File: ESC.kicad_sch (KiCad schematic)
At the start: 2 parts, among them U5 STM32G071GBUxN

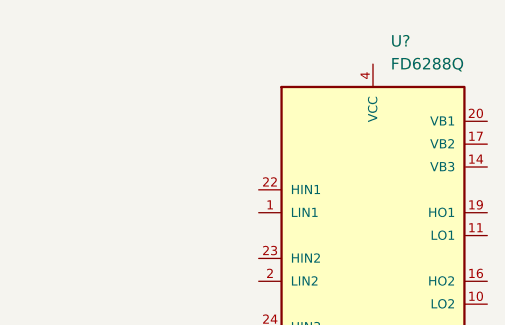
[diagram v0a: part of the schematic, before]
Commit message: Receiver design
Updated the receiver design for the SX1280.
Added an ignore for lock files.
Minor schematic updates.
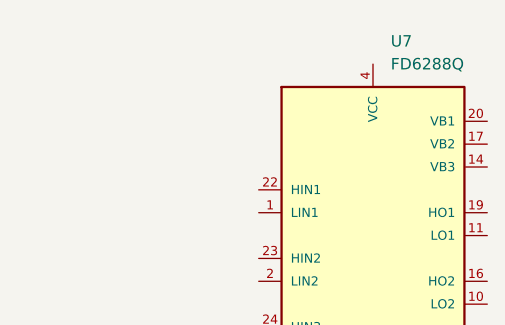
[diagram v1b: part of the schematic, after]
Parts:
- U5: footprint Package_DFN_QFN:QFN-28_4x4mm_P0.5mm -> Custom_Parts:QFN-28_4x4mm_P0.5mm
- gave numbers to parts that had none: 1
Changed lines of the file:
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@@
 		(dnp no)
 		(fields_autoplaced yes)
-		(property "Reference" "U?"
+		(property "Reference" "U7"
 			(at 123.8886 34.29 0)
 			(effects
@@
 			(project "ThunderHorse"
 				(path "/ac187c6c-fa53-41cc-bce1-6f39a42a92e8/807a5f6f-4255-4cf0-8d90-acd62bb18590"
-					(reference "U?")
+					(reference "U7")
 					(unit 1)
 				)
@@
 			)
 		)
-		(property "Footprint" "Package_DFN_QFN:QFN-28_4x4mm_P0.5mm"
+		(property "Footprint" "Custom_Parts:QFN-28_4x4mm_P0.5mm"
 			(at 44.45 86.36 0)
 			(effects

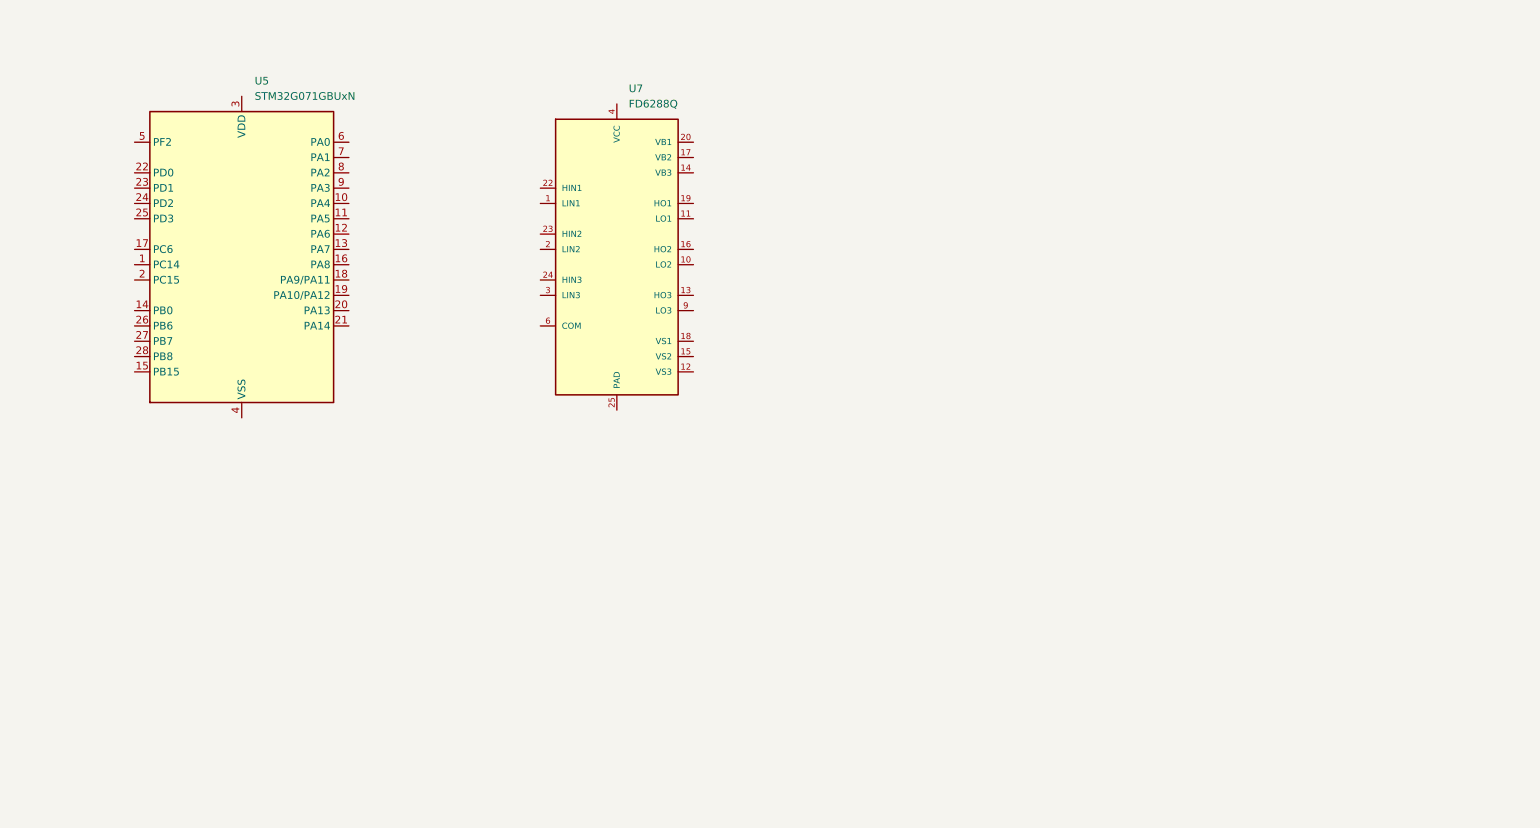
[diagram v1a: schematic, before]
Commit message: ESC design
Updated the ESC schematic.
Replaces the INA 226 with INA230.
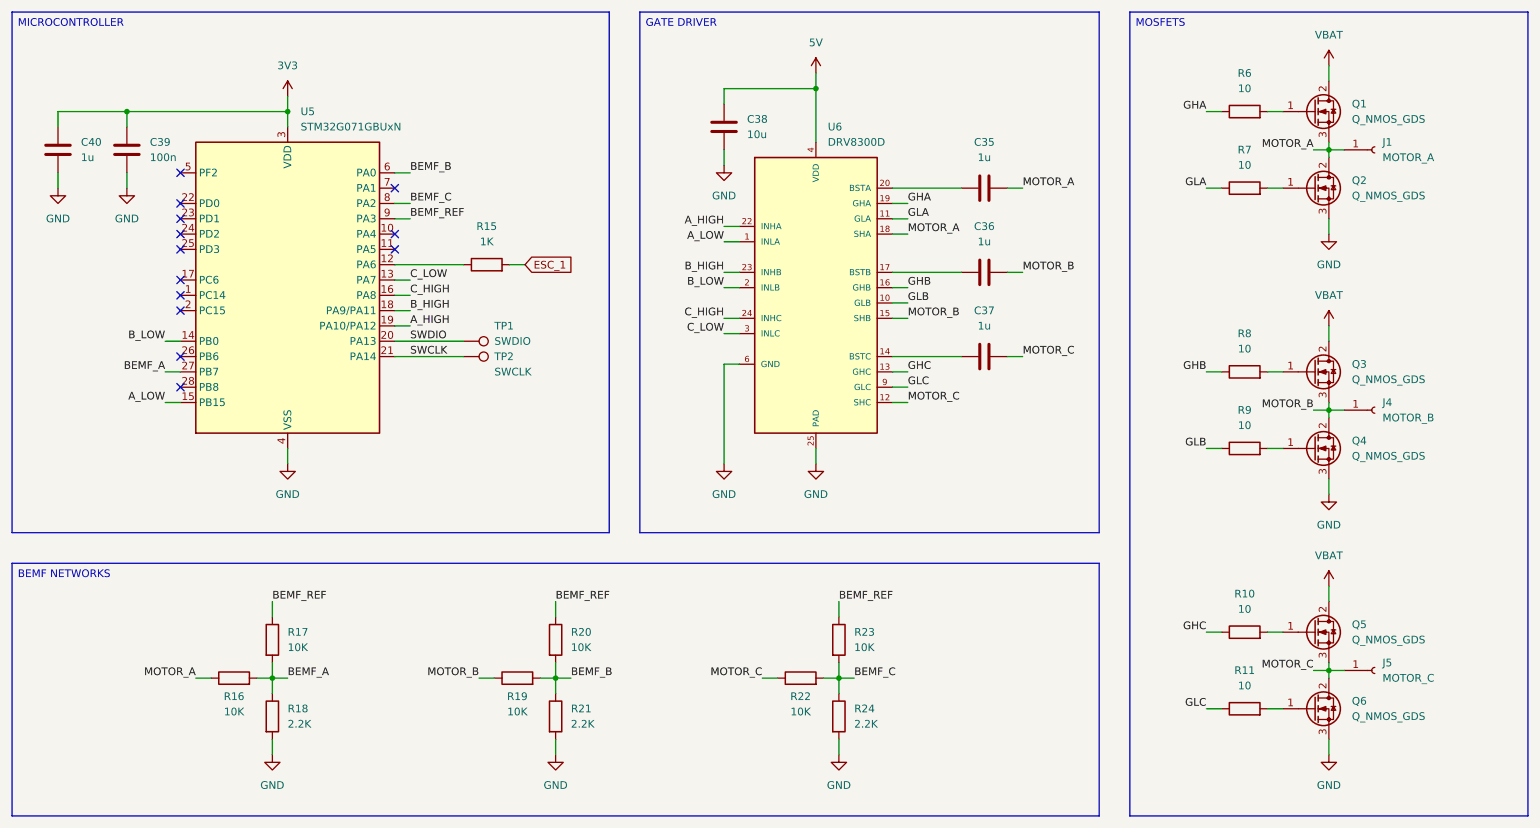
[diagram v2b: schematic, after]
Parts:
- removed U7: FD6288Q, Custom_Parts:FD6288Q, symbol Custom_Parts:FD6288Q
- added C35, C36, C37, C40: 1u, symbol Device:C
- added C38: 10u, symbol Device:C
- added C39: 100n, symbol Device:C
- added J1: MOTOR_A, TestPoint:TestPoint_Pad_D2.0mm, symbol Connector:Conn_01x01_Socket
- added J4: MOTOR_B, TestPoint:TestPoint_Pad_D2.0mm, symbol Connector:Conn_01x01_Socket
- added J5: MOTOR_C, TestPoint:TestPoint_Pad_D2.0mm, symbol Connector:Conn_01x01_Socket
- added Q1, Q2, Q3, Q4, Q5, Q6: Q_NMOS_GDS, symbol Transistor_FET:Q_NMOS_GDS
- added R10, R11, R6, R7, R8, R9: 10, symbol Device:R
- added R15: 1K, symbol Device:R
- added R16, R17, R19, R20, R22, R23: 10K, symbol Device:R
- added R18, R21, R24: 2.2K, symbol Device:R
- added TP1: SWDIO, TestPoint:TestPoint_Pad_D1.0mm, symbol Connector:TestPoint
- added TP2: SWCLK, TestPoint:TestPoint_Pad_D1.0mm, symbol Connector:TestPoint
- added U6: DRV8300D, Custom_Parts:VQFN-24-1EP_4x4mm_P0.5mm_EP2.45x2.45mm, symbol Custom_Parts:DRV8300D
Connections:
- net at U5.12 (PA6): now also R15.1
- net C_LOW: now reaches U5.13 (PA7)
- net C_LOW: now also U6.3 (INLC)
- net B_LOW: now reaches U5.14 (PB0)
- net B_LOW: now also U6.2 (INLB)
- net A_LOW: now reaches U5.15 (PB15)
- net A_LOW: now also U6.1 (INLA)
- net C_HIGH: now reaches U5.16 (PA8)
- net C_HIGH: now also U6.24 (INHC)
- net B_HIGH: now reaches U5.18 (PA9/PA11)
- net B_HIGH: now also U6.23 (INHB)
- net A_HIGH: now reaches U5.19 (PA10/PA12)
- net A_HIGH: now also U6.22 (INHA)
- net SWDIO: now reaches U5.20 (PA13)
- net SWDIO: now also TP1.1
- net SWCLK: now reaches U5.21 (PA14)
- net SWCLK: now also TP2.1
- net BEMF_A: now reaches U5.27 (PB7)
- net BEMF_A: now also R16.2, R17.2, R18.1
- net 3V3: now reaches U5.3 (VDD)
- net 3V3: now also C39.1, C40.1
- net GND: now reaches U5.4 (VSS)
- net GND: now also C38.2, C39.2, C40.2, Q2.3 (S), Q4.3 (S), Q6.3 (S), R18.2, R21.2, R24.2, U6.25 (PAD), U6.6 (GND)
- net BEMF_B: now reaches U5.6 (PA0)
- net BEMF_B: now also R19.2, R20.2, R21.1
- net BEMF_C: now reaches U5.8 (PA2)
- net BEMF_C: now also R22.2, R23.2, R24.1
- net BEMF_REF: now reaches U5.9 (PA3)
- net BEMF_REF: now also R17.1, R20.1, R23.1
- new net: C36.1, U6.17 (BSTB)
- new net: Q3.1 (G), R8.2
- new net: C37.1, U6.14 (BSTC)
- new net: Q4.1 (G), R9.2
- new net: Q5.1 (G), R10.2
- new net: C35.1, U6.20 (BSTA)
- new net: Q6.1 (G), R11.2
- new net: Q2.1 (G), R7.2
- new net: Q1.1 (G), R6.2
- new net 5V: C38.1, U6.4 (VDD)
- new net ESC_1: R15.2
- new net GHA: R6.1, U6.19 (GHA)
- new net GHB: R8.1, U6.16 (GHB)
- new net GHC: R10.1, U6.13 (GHC)
- new net GLA: R7.1, U6.11 (GLA)
- new net GLB: R9.1, U6.10 (GLB)
- new net GLC: R11.1, U6.9 (GLC)
- new net MOTOR_A: C35.2, J1.1 (Pin_1), Q1.3 (S), Q2.2 (D), R16.1, U6.18 (SHA)
- new net MOTOR_B: C36.2, J4.1 (Pin_1), Q3.3 (S), Q4.2 (D), R19.1, U6.15 (SHB)
- new net MOTOR_C: C37.2, J5.1 (Pin_1), Q5.3 (S), Q6.2 (D), R22.1, U6.12 (SHC)
- new net VBAT: Q1.2 (D), Q3.2 (D), Q5.2 (D)
- no-connect marks 0 -> 13

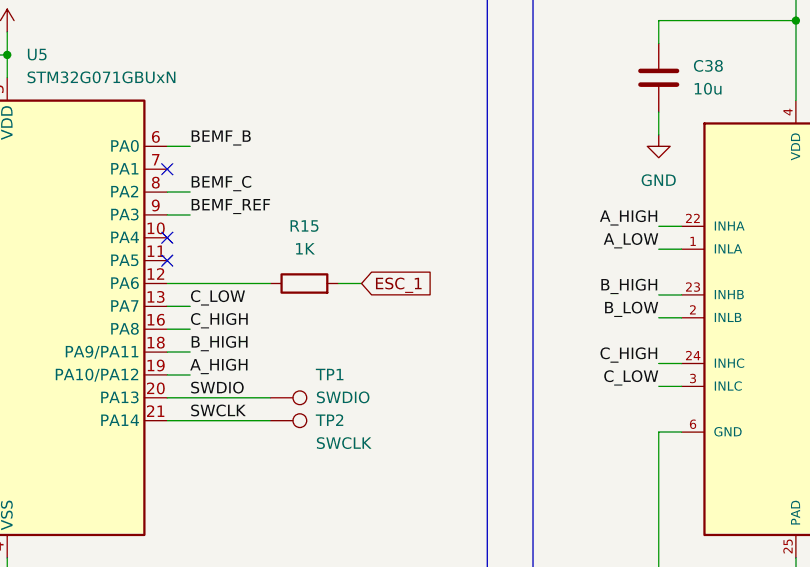
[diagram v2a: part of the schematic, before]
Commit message: MCU design
Updated the main RP2350 schematic.
Updated labels for other designs.
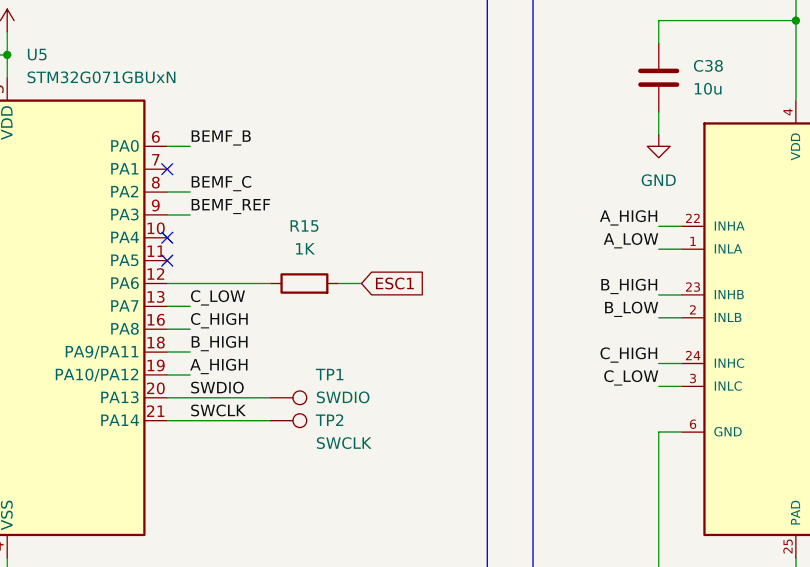
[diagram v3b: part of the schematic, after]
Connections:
- net ESC_1 renamed ESC1
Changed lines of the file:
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@@
 		)
 	)
-	(global_label "ESC_1"
+	(global_label "ESC1"
 		(shape input)
 		(at 106.68 63.5 0)
@@
 		)
 		(property "Intersheetrefs" "${INTERSHEET_REFS}"
-			(at 115.4708 63.5 0)
+			(at 114.5032 63.5 0)
 			(effects
 				(font

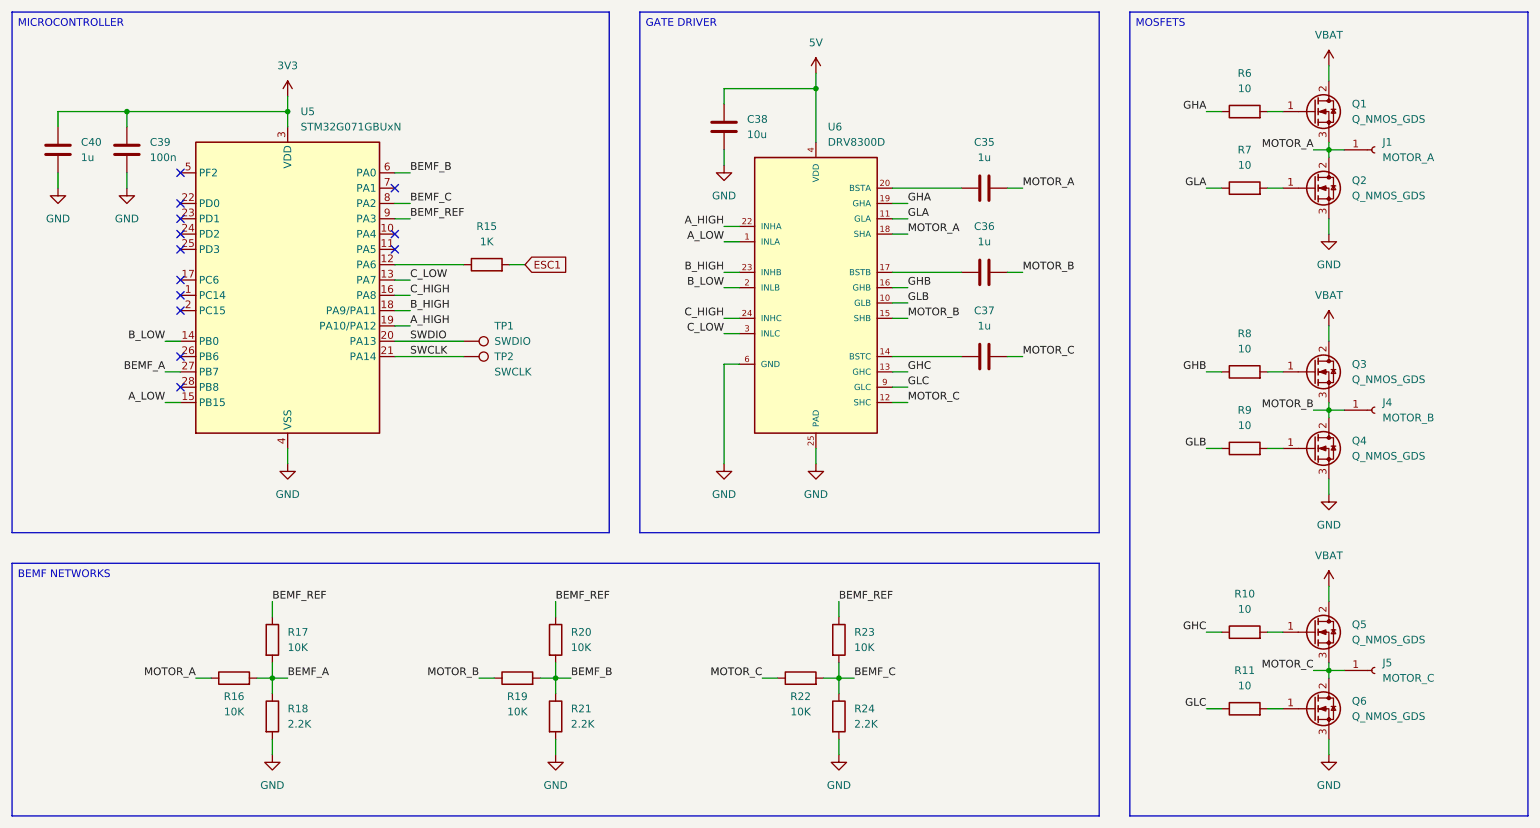
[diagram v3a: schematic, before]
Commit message: Complete ESC and MCU
Added the 4 ESC to the eschematic.
Updated the MCU design to add the connectors and buzzer.
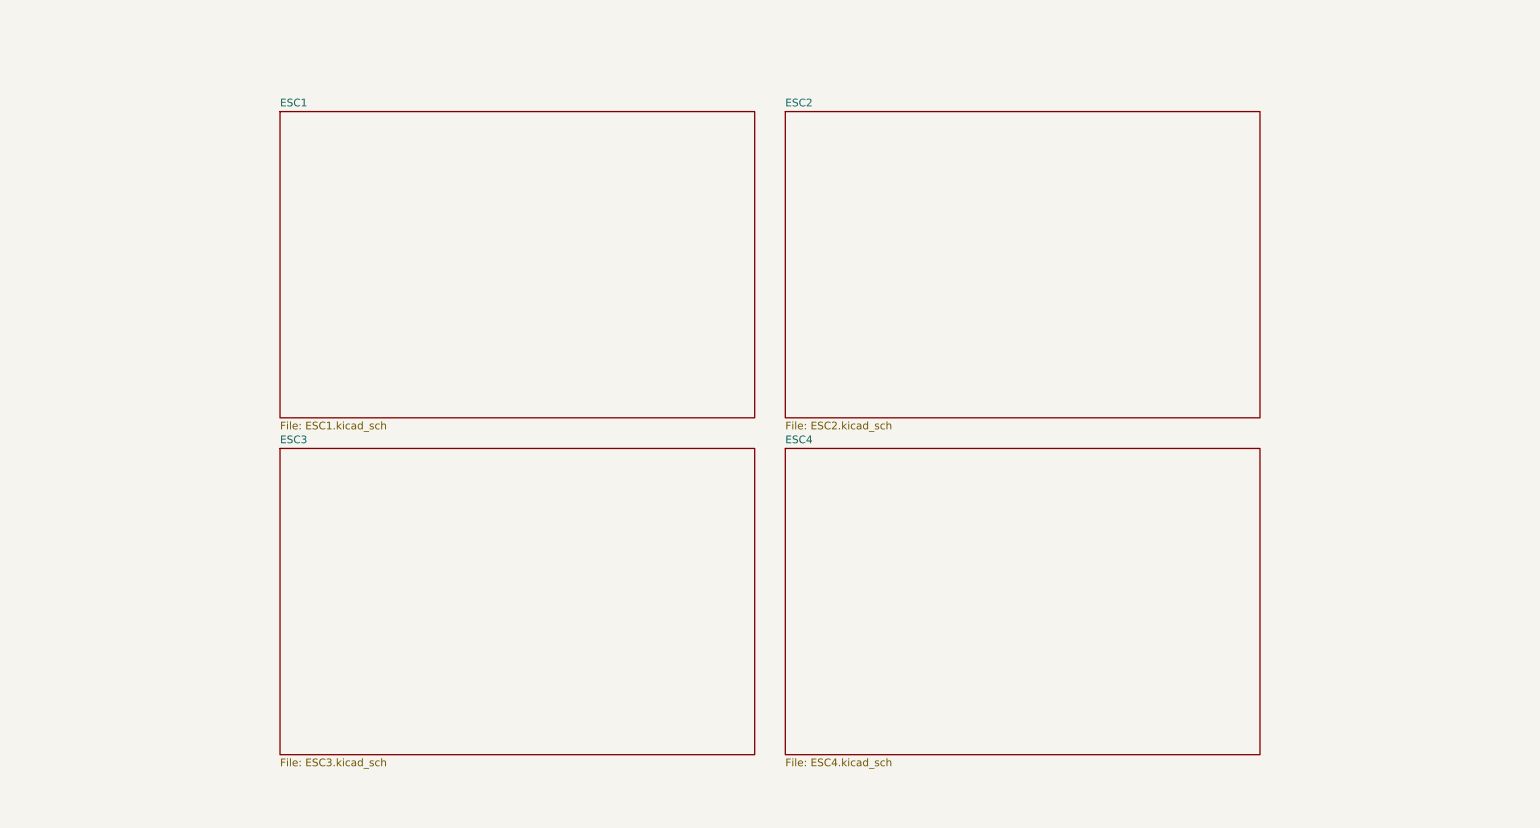
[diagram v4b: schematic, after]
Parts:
- removed C35, C36, C37, C40: 1u, symbol Device:C
- removed C38: 10u, symbol Device:C
- removed C39: 100n, symbol Device:C
- removed J1: MOTOR_A, TestPoint:TestPoint_Pad_D2.0mm, symbol Connector:Conn_01x01_Socket
- removed J4: MOTOR_B, TestPoint:TestPoint_Pad_D2.0mm, symbol Connector:Conn_01x01_Socket
- removed J5: MOTOR_C, TestPoint:TestPoint_Pad_D2.0mm, symbol Connector:Conn_01x01_Socket
- removed Q1, Q2, Q3, Q4, Q5, Q6: Q_NMOS_GDS, symbol Transistor_FET:Q_NMOS_GDS
- removed R10, R11, R6, R7, R8, R9: 10, symbol Device:R
- removed R15: 1K, symbol Device:R
- removed R16, R17, R19, R20, R22, R23: 10K, symbol Device:R
- removed R18, R21, R24: 2.2K, symbol Device:R
- removed TP1: SWDIO, TestPoint:TestPoint_Pad_D1.0mm, symbol Connector:TestPoint
- removed TP2: SWCLK, TestPoint:TestPoint_Pad_D1.0mm, symbol Connector:TestPoint
- removed U5: STM32G071GBUxN, Custom_Parts:QFN-28_4x4mm_P0.5mm, symbol MCU_ST_STM32G0:STM32G071GBUxN
- removed U6: DRV8300D, Custom_Parts:VQFN-24-1EP_4x4mm_P0.5mm_EP2.45x2.45mm, symbol Custom_Parts:DRV8300D
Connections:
- no-connect marks 13 -> 0
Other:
- added sheet ESC1 (ESC1.kicad_sch)
- added sheet ESC2 (ESC2.kicad_sch)
- added sheet ESC3 (ESC3.kicad_sch)
- added sheet ESC4 (ESC4.kicad_sch)
